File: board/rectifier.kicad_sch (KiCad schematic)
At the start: 4 parts

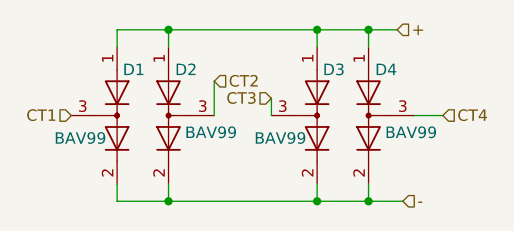
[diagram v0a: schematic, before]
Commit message: fixed reverse polarity bug
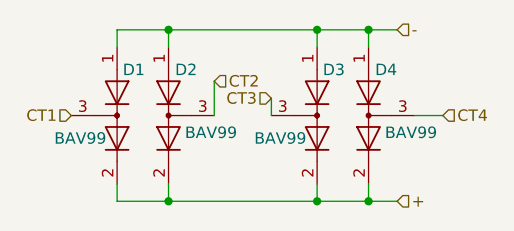
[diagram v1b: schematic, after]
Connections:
- net +: now also D1.2 (A), D2.2 (A), D3.2 (A), D4.2 (A); no longer D1.1 (K), D2.1 (K), D3.1 (K), D4.1 (K)
- net -: now also D1.1 (K), D2.1 (K), D3.1 (K), D4.1 (K); no longer D1.2 (A), D2.2 (A), D3.2 (A), D4.2 (A)
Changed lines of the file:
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@@
-(kicad_sch (version 20211123) (generator eeschema)
+(kicad_sch (version 20230121) (generator eeschema)
   (paper "A4")
   (junction (at 157.48 127) (diameter 0) (color 0 0 0 0)
@@
   )
   (wire (pts (xy 168.275 117.475) (xy 171.45 117.475))
-    (stroke (width 0) (type default) (color 0 0 0 0))
+    (stroke (width 0) (type default))
   )
   (wire (pts (xy 157.48 109.855) (xy 157.48 107.95))
-    (stroke (width 0) (type default) (color 0 0 0 0))
+    (stroke (width 0) (type default))
   )
   (wire (pts (xy 135.255 107.95) (xy 140.97 107.95))
-    (stroke (width 0) (type default) (color 0 0 0 0))
+    (stroke (width 0) (type default))
   )
   (wire (pts (xy 163.195 127) (xy 163.195 125.095))
-    (stroke (width 0) (type default) (color 0 0 0 0))
+    (stroke (width 0) (type default))
   )
   (wire (pts (xy 135.255 109.855) (xy 135.255 107.95))
-    (stroke (width 0) (type default) (color 0 0 0 0))
+    (stroke (width 0) (type default))
   )
   (wire (pts (xy 140.97 127) (xy 157.48 127))
-    (stroke (width 0) (type default) (color 0 0 0 0))
+    (stroke (width 0) (type default))
   )
   (wire (pts (xy 140.97 107.95) (xy 157.48 107.95))
-    (stroke (width 0) (type default) (color 0 0 0 0))
+    (stroke (width 0) (type default))
   )
   (wire (pts (xy 135.255 127) (xy 140.97 127))
-    (stroke (width 0) (type default) (color 0 0 0 0))
+    (stroke (width 0) (type default))
   )
   (wire (pts (xy 157.48 107.95) (xy 163.195 107.95))
-    (stroke (width 0) (type default) (color 0 0 0 0))
+    (stroke (width 0) (type default))
   )
   (wire (pts (xy 163.195 107.95) (xy 166.37 107.95))
-    (stroke (width 0) (type default) (color 0 0 0 0))
+    (stroke (width 0) (type default))
   )
   (wire (pts (xy 152.4 115.57) (xy 152.4 117.475))
-    (stroke (width 0) (type default) (color 0 0 0 0))
+    (stroke (width 0) (type default))
   )
-  (wire (pts (xy 163.195 127) (xy 167.005 127))
-    (stroke (width 0) (type default) (color 0 0 0 0))
+  (wire (pts (xy 163.195 127) (xy 166.37 127))
+    (stroke (width 0) (type default))
   )
   (wire (pts (xy 157.48 125.095) (xy 157.48 127))
-    (stroke (width 0) (type default) (color 0 0 0 0))
+    (stroke (width 0) (type default))
   )
   (wire (pts (xy 140.97 107.95) (xy 140.97 109.855))
-    (stroke (width 0) (type default) (color 0 0 0 0))
+    (stroke (width 0) (type default))
   )
   (wire (pts (xy 146.05 113.665) (xy 146.05 117.475))
-    (stroke (width 0) (type default) (color 0 0 0 0))
+    (stroke (width 0) (type default))
   )
   (wire (pts (xy 157.48 127) (xy 163.195 127))
-    (stroke (width 0) (type default) (color 0 0 0 0))
+    (stroke (width 0) (type default))
   )
   (wire (pts (xy 163.195 107.95) (xy 163.195 109.855))
-    (stroke (width 0) (type default) (color 0 0 0 0))
+    (stroke (width 0) (type default))
   )
   (wire (pts (xy 135.255 125.095) (xy 135.255 127))
-    (stroke (width 0) (type default) (color 0 0 0 0))
+    (stroke (width 0) (type default))
   )
   (wire (pts (xy 140.97 127) (xy 140.97 125.095))
-    (stroke (width 0) (type default) (color 0 0 0 0))
+    (stroke (width 0) (type default))
   )
-  (hierarchical_label "+" (shape input) (at 166.37 107.95 0)
+  (hierarchical_label "+" (shape input) (at 166.37 127 0) (fields_autoplaced)
     (effects (font (size 1.27 1.27)) (justify left))
   )
-  (hierarchical_label "CT2" (shape input) (at 146.05 113.665 0)
+  (hierarchical_label "CT2" (shape input) (at 146.05 113.665 0) (fields_autoplaced)
     (effects (font (size 1.27 1.27)) (justify left))
   )
-  (hierarchical_label "CT4" (shape input) (at 171.45 117.475 0)
+  (hierarchical_label "CT4" (shape input) (at 171.45 117.475 0) (fields_autoplaced)
     (effects (font (size 1.27 1.27)) (justify left))
   )
-  (hierarchical_label "-" (shape input) (at 167.005 127 0)
+  (hierarchical_label "-" (shape input) (at 166.37 107.95 0) (fields_autoplaced)
     (effects (font (size 1.27 1.27)) (justify left))
   )
-  (hierarchical_label "CT1" (shape input) (at 130.175 117.475 180)
+  (hierarchical_label "CT1" (shape input) (at 130.175 117.475 180) (fields_autoplaced)
     (effects (font (size 1.27 1.27)) (justify right))
   )
-  (hierarchical_label "CT3" (shape input) (at 152.4 115.57 180)
+  (hierarchical_label "CT3" (shape input) (at 152.4 115.57 180) (fields_autoplaced)
     (effects (font (size 1.27 1.27)) (justify right))
   )
   (symbol (lib_id "Diode:BAV99") (at 135.255 117.475 270) (unit 1)
-    (in_bom yes) (on_board yes)
-    (property "Reference" "D1" (id 0) (at 135.89 112.395 90)
+    (in_bom yes) (on_board yes) (dnp no)
+    (property "Reference" "D1" (at 135.89 112.395 90)
       (effects (font (size 1.27 1.27)) (justify left))
     )
-    (property "Value" "BAV99" (id 1) (at 128.27 120.015 90)
+    (property "Value" "BAV99" (at 128.27 120.015 90)
       (effects (font (size 1.27 1.27)) (justify left))
     )
-    (property "Footprint" "Package_TO_SOT_SMD:SOT-23" (id 2) (at 122.555 117.475 0)
+    (property "Footprint" "Package_TO_SOT_SMD:SOT-23" (at 122.555 117.475 0)
       (effects (font (size 1.27 1.27)) hide)
     )
-    (property "Datasheet" "https://assets.nexperia.com/documents/data-sheet/BAV99_SER.pdf" (id 3) (at 135.255 117.475 0)
+    (property "Datasheet" "https://assets.nexperia.com/documents/data-sheet/BAV99_SER.pdf" (at 135.255 117.475 0)
       (effects (font (size 1.27 1.27)) hide)
     )
@@
     (pin "2")
     (pin "3")
+    (instances
+      (project "board"
+        (path "/57732dd3-1162-4c3f-88bd-31bf473d124d/767ce4c6-0e55-4543-92f0-34cb8237a544"
+          (reference "D1") (unit 1)
+        )
+      )
+    )
   )
   (symbol (lib_id "Diode:BAV99") (at 163.195 117.475 90) (mirror x) (unit 1)
-    (in_bom yes) (on_board yes)
-    (property "Reference" "D4" (id 0) (at 166.37 112.395 90)
+    (in_bom yes) (on_board yes) (dnp no)
+    (property "Reference" "D4" (at 166.37 112.395 90)
       (effects (font (size 1.27 1.27)) (justify left))
     )
-    (property "Value" "BAV99" (id 1) (at 170.815 119.38 90)
+    (property "Value" "BAV99" (at 170.815 119.38 90)
       (effects (font (size 1.27 1.27)) (justify left))
     )
-    (property "Footprint" "Package_TO_SOT_SMD:SOT-23" (id 2) (at 175.895 117.475 0)
+    (property "Footprint" "Package_TO_SOT_SMD:SOT-23" (at 175.895 117.475 0)
       (effects (font (size 1.27 1.27)) hide)
     )
-    (property "Datasheet" "https://assets.nexperia.com/documents/data-sheet/BAV99_SER.pdf" (id 3) (at 163.195 117.475 0)
+    (property "Datasheet" "https://assets.nexperia.com/documents/data-sheet/BAV99_SER.pdf" (at 163.195 117.475 0)
       (effects (font (size 1.27 1.27)) hide)
     )
@@
     (pin "2")
     (pin "3")
+    (instances
+      (project "board"
+        (path "/57732dd3-1162-4c3f-88bd-31bf473d124d/767ce4c6-0e55-4543-92f0-34cb8237a544"
+          (reference "D4") (unit 1)
+        )
+      )
+    )
   )
   (symbol (lib_id "Diode:BAV99") (at 140.97 117.475 90) (mirror x) (unit 1)
-    (in_bom yes) (on_board yes)
-    (property "Reference" "D2" (id 0) (at 144.145 112.395 90)
+    (in_bom yes) (on_board yes) (dnp no)
+    (property "Reference" "D2" (at 144.145 112.395 90)
       (effects (font (size 1.27 1.27)) (justify left))
     )
-    (property "Value" "BAV99" (id 1) (at 148.59 119.38 90)
+    (property "Value" "BAV99" (at 148.59 119.38 90)
       (effects (font (size 1.27 1.27)) (justify left))
     )
-    (property "Footprint" "Package_TO_SOT_SMD:SOT-23" (id 2) (at 153.67 117.475 0)
+    (property "Footprint" "Package_TO_SOT_SMD:SOT-23" (at 153.67 117.475 0)
       (effects (font (size 1.27 1.27)) hide)
     )
-    (property "Datasheet" "https://assets.nexperia.com/documents/data-sheet/BAV99_SER.pdf" (id 3) (at 140.97 117.475 0)
+    (property "Datasheet" "https://assets.nexperia.com/documents/data-sheet/BAV99_SER.pdf" (at 140.97 117.475 0)
       (effects (font (size 1.27 1.27)) hide)
     )
@@
     (pin "2")
     (pin "3")
+    (instances
+      (project "board"
+        (path "/57732dd3-1162-4c3f-88bd-31bf473d124d/767ce4c6-0e55-4543-92f0-34cb8237a544"
+          (reference "D2") (unit 1)
+        )
+      )
+    )
   )
   (symbol (lib_id "Diode:BAV99") (at 157.48 117.475 270) (unit 1)
-    (in_bom yes) (on_board yes)
-    (property "Reference" "D3" (id 0) (at 158.115 112.395 90)
+    (in_bom yes) (on_board yes) (dnp no)
+    (property "Reference" "D3" (at 158.115 112.395 90)
       (effects (font (size 1.27 1.27)) (justify left))
     )
-    (property "Value" "BAV99" (id 1) (at 150.495 120.015 90)
+    (property "Value" "BAV99" (at 150.495 120.015 90)
       (effects (font (size 1.27 1.27)) (justify left))
     )
-    (property "Footprint" "Package_TO_SOT_SMD:SOT-23" (id 2) (at 144.78 117.475 0)
+    (property "Footprint" "Package_TO_SOT_SMD:SOT-23" (at 144.78 117.475 0)
       (effects (font (size 1.27 1.27)) hide)
     )
-    (property "Datasheet" "https://assets.nexperia.com/documents/data-sheet/BAV99_SER.pdf" (id 3) (at 157.48 117.475 0)
+    (property "Datasheet" "https://assets.nexperia.com/documents/data-sheet/BAV99_SER.pdf" (at 157.48 117.475 0)
       (effects (font (size 1.27 1.27)) hide)
     )
@@
     (pin "2")
     (pin "3")
+    (instances
+      (project "board"
+        (path "/57732dd3-1162-4c3f-88bd-31bf473d124d/767ce4c6-0e55-4543-92f0-34cb8237a544"
+          (reference "D3") (unit 1)
+        )
+      )
+    )
   )
 )
